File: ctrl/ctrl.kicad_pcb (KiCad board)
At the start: 2 copper layers, 38.9 x 61 mm, 17 parts, among them J1 Conn_01x20, J2 Conn_01x20, J3 Conn_01x20, J4 Conn_01x20

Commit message: pcb: Update revision numbers
Signed-off-by: Dylan Turner <dylan.turner@tutanota.com>
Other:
- board text added: "r3"
- board text removed: "r2"
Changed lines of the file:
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@@
 	(title_block
 		(title "PS-OHK Control Board")
-		(date "2024-06-24")
-		(rev "2")
+		(date "2024-06-25")
+		(rev "3")
 		(company "Polymath-Studio")
 	)
@@
 		)
 	)
-	(gr_text "r2"
-		(at 36.576 56.134 -90)
+	(gr_text "r3"
+		(at 36.576 56.134 270)
 		(layer "B.SilkS")
 		(effects

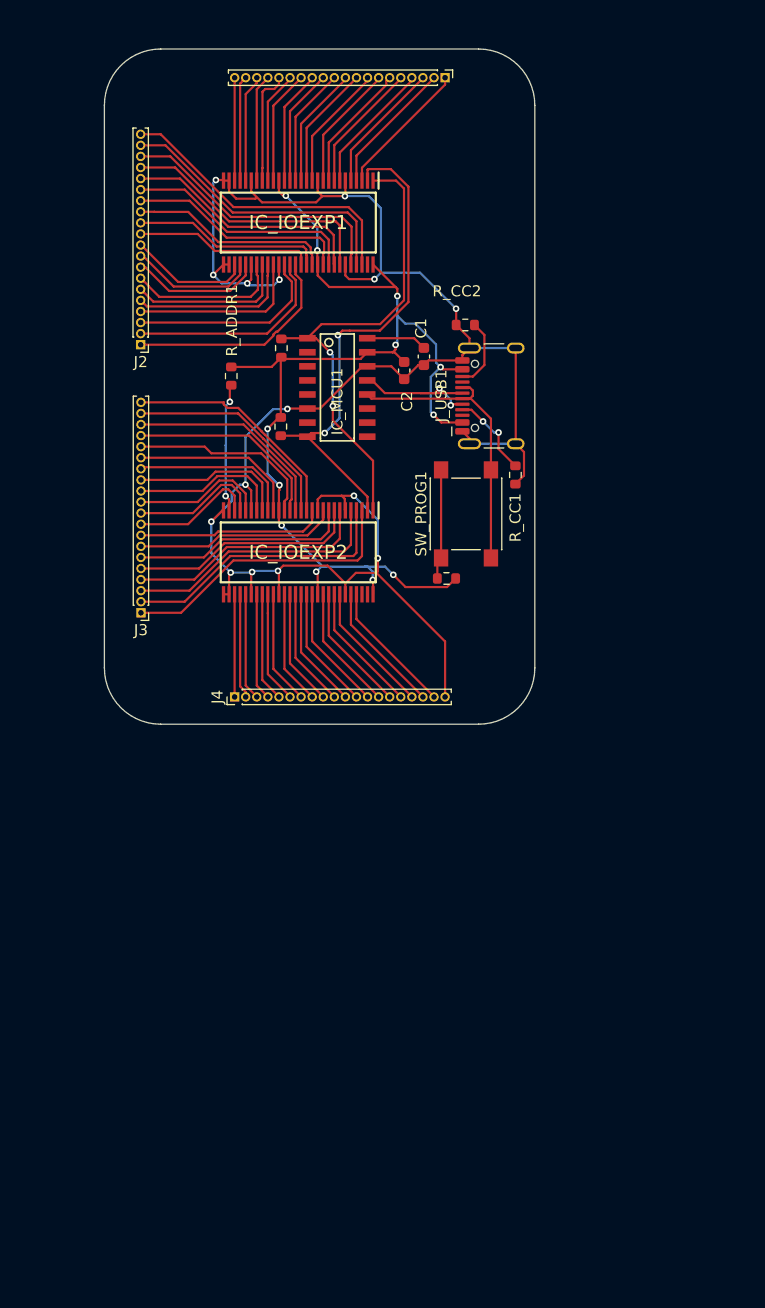
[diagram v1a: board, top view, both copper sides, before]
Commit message: r4: 1mm->2.54mm pins, no right-hand yet
Signed-off-by: Dylan Turner <dylan.turner@tutanota.com>
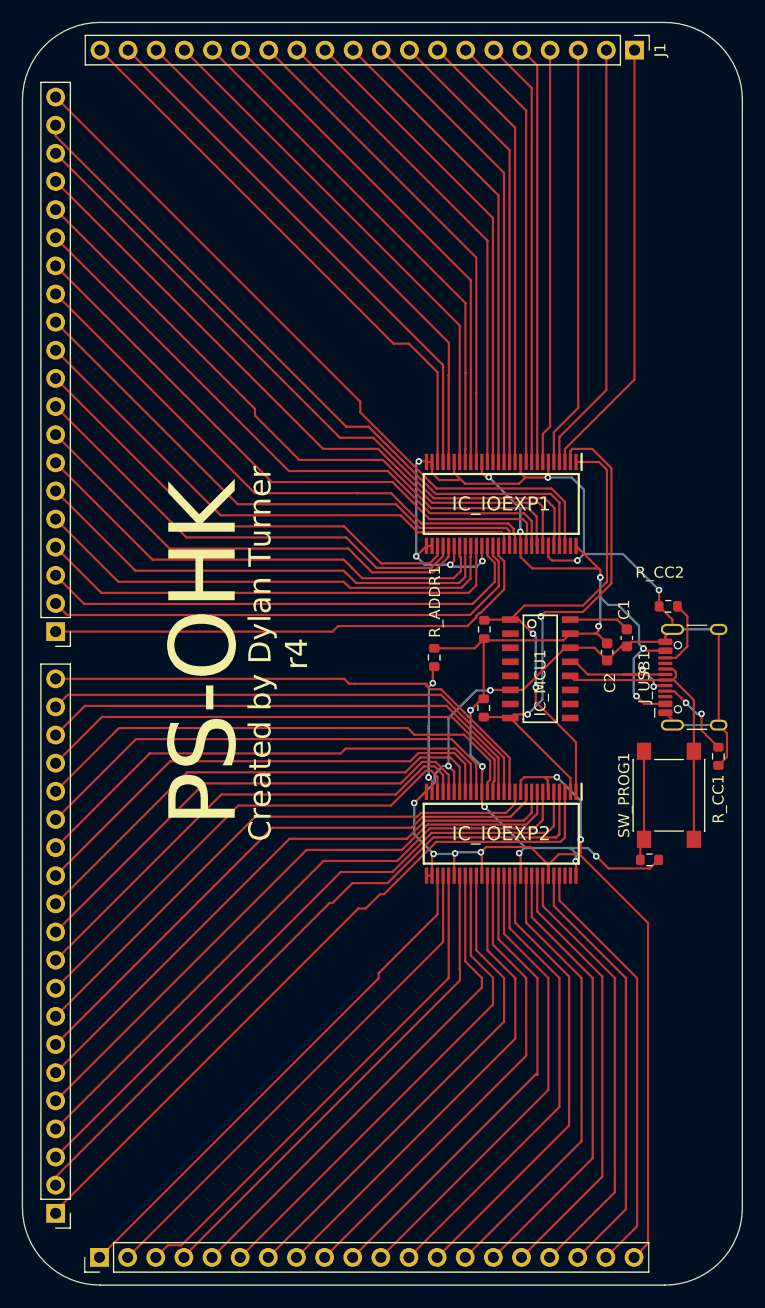
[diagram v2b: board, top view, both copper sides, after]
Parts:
- J1, J2, J3, J4: footprint Connector_PinHeader_1.00mm:PinHeader_1x20_P1.00mm_Vertical -> Connector_PinHeader_2.54mm:PinHeader_1x20_P2.54mm_Vertical
- moved J3 54.8 mm to (21.0, 130.5)
- moved J4 52.1 mm to (25.0, 134.5)
- moved IC_IOEXP1 31.3 mm to (61.2, 66.5)
- moved IC_IOEXP2 31.3 mm to (61.2, 96.2)
- moved R_ADDR1 31.3 mm to (55.2, 80.3)
- moved R_I2C1 31.3 mm to (59.7, 77.8)
- moved R_PROG1 31.3 mm to (74.6, 98.6)
- moved J_USB1 31.3 mm to (79.8, 82.1)
- moved R_CC1 31.3 mm to (80.8, 89.3)
- moved C1 31.3 mm to (72.6, 78.6)
- moved R_I2C2 31.3 mm to (59.6, 84.9)
- moved SW_PROG1 31.3 mm to (76.4, 92.8)
- moved C2 31.3 mm to (70.8, 79.8)
- moved IC_MCU1 31.3 mm to (64.8, 81.4)
- moved R_CC2 31.3 mm to (76.3, 75.7)
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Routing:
- net /KEY_PGU: track 9.29 -> 50.6 mm
- net /KEY_HOM: track 9.50 -> 49.0 mm
- net /KEY_K: track 27.2 -> 65.6 mm
- net /KEY_INS: track 9.71 -> 48.1 mm
- net /KEY_G: track 26.2 -> 64.3 mm
- net /KEY_X: track 26.2 -> 64.1 mm
- net /KEY_A: track 9.27 -> 47.1 mm
- net /KEY_RIGHT: track 9.71 -> 47.5 mm
- net /KEY_L: track 25.1 -> 62.9 mm
- net /KEY_8: track 9.47 -> 46.3 mm
- net /KEY_R: track 23.8 -> 60.5 mm
- net /KEY_3: track 25.1 -> 61.7 mm
- net /KEY_9: track 9.68 -> 46.1 mm
- net /KEY_LEFT: track 10.4 -> 46.7 mm
- net /KEY_4: track 22.0 -> 58.1 mm
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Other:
- board size 38.9 x 61 mm -> 65 x 114 mm
- board text added: "r4"
- board text removed: "r3"
